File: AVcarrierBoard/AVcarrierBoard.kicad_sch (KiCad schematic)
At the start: 10 parts, among them J1 QuarkScrewTerminal, J2 Screw_Terminal_01x04, J3 Screw_Terminal_01x04, J4 Mech_Switch, J5 Mech_Switch, U1 EggfinderMini/FeatherGPS, U2 EggtimerQuark, U3 Blue_Raven

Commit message: LOST FILES HAHAAHAHA
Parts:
- BT1: value Battery -> Batt_2S; footprint (none) -> COTS_Boards:BAT_1048P
- BT2: value Battery_Cell -> Batt_1S; footprint (none) -> COTS_Boards:1042P_KEY
- J1: value QuarkScrewTerminal -> QuarkRecov; footprint (none) -> COTS_Boards:ScrewTerminals_2828362
- J2: value Screw_Terminal_01x04 -> RavenStaging; footprint (none) -> COTS_Boards:ScrewTerminals_2828362
- J3: value Screw_Terminal_01x04 -> RavenRecov; footprint (none) -> COTS_Boards:ScrewTerminals_2828362
- J4, J5: footprint (none) -> Connector_PinHeader_2.54mm:PinHeader_1x02_P2.54mm_Vertical
- U2: footprint (none) -> COTS_Boards:EggtimerQuark
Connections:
- net BATT_1S: now also J2.2 (Pin_2), J2.4 (Pin_4), J3.2 (Pin_2), J3.4 (Pin_4)
- net RavenAPO: now reaches U3.3 (Apo)
- net RavenAPO: now also J3.3 (Pin_3)
- net RavenMAIN: now reaches U3.4 (Main)
- net RavenMAIN: now also J3.1 (Pin_1)
- net Raven3RD: now reaches U3.5 (3rd)
- net Raven3RD: now also J2.3 (Pin_3)
- net Raven4TH: now reaches U3.6 (4th)
- net Raven4TH: now also J2.1 (Pin_1)
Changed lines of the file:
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@@
+    )
+  )
+  (global_label "Raven3RD" (shape input) (at 135.89 106.68 0) (fields_autoplaced)
+    (effects (font (size 1.27 1.27)) (justify left))
+    (property "Intersheetrefs" "${INTERSHEET_REFS}" (at 148.2489 106.68 0)
+      (effects (font (size 1.27 1.27)) (justify left) hide)
+    )
+  )
+  (global_label "BATT_1S" (shape input) (at 166.37 113.03 180) (fields_autoplaced)
+    (effects (font (size 1.27 1.27)) (justify right))
+    (property "Intersheetrefs" "${INTERSHEET_REFS}" (at 155.7044 113.03 0)
+      (effects (font (size 1.27 1.27)) (justify right) hide)
+    )
+  )
+  (global_label "RavenAPO" (shape input) (at 135.89 111.76 0) (fields_autoplaced)
+    (effects (font (size 1.27 1.27)) (justify left))
+    (property "Intersheetrefs" "${INTERSHEET_REFS}" (at 148.1885 111.76 0)
+      (effects (font (size 1.27 1.27)) (justify left) hide)
+    )
+  )
+  (global_label "RavenAPO" (shape input) (at 166.37 110.49 180) (fields_autoplaced)
+    (effects (font (size 1.27 1.27)) (justify right))
+    (property "Intersheetrefs" "${INTERSHEET_REFS}" (at 154.0715 110.49 0)
+      (effects (font (size 1.27 1.27)) (justify right) hide)
+    )
+  )
+  (global_label "RavenMAIN" (shape input) (at 166.37 105.41 180) (fields_autoplaced)
+    (effects (font (size 1.27 1.27)) (justify right))
+    (property "Intersheetrefs" "${INTERSHEET_REFS}" (at 153.2853 105.41 0)
+      (effects (font (size 1.27 1.27)) (justify right) hide)
+    )
+  )
+  (global_label "BATT_1S" (shape input) (at 166.37 90.17 180) (fields_autoplaced)
+    (effects (font (size 1.27 1.27)) (justify right))
+    (property "Intersheetrefs" "${INTERSHEET_REFS}" (at 155.7044 90.17 0)
+      (effects (font (size 1.27 1.27)) (justify right) hide)
     )
   )
@@
     )
   )
+  (global_label "Raven4TH" (shape input) (at 166.37 87.63 180) (fields_autoplaced)
+    (effects (font (size 1.27 1.27)) (justify right))
+    (property "Intersheetrefs" "${INTERSHEET_REFS}" (at 154.253 87.63 0)
+      (effects (font (size 1.27 1.27)) (justify right) hide)
+    )
+  )
   (global_label "MAIN2" (shape input) (at 132.08 68.58 0) (fields_autoplaced)
     (effects (font (size 1.27 1.27)) (justify left))
@@
     )
   )
+  (global_label "BATT_1S" (shape input) (at 166.37 95.25 180) (fields_autoplaced)
+    (effects (font (size 1.27 1.27)) (justify right))
+    (property "Intersheetrefs" "${INTERSHEET_REFS}" (at 155.7044 95.25 0)
+      (effects (font (size 1.27 1.27)) (justify right) hide)
+    )
+  )
+  (global_label "Raven3RD" (shape input) (at 166.37 92.71 180) (fields_autoplaced)
+    (effects (font (size 1.27 1.27)) (justify right))
+    (property "Intersheetrefs" "${INTERSHEET_REFS}" (at 154.0111 92.71 0)
+      (effects (font (size 1.27 1.27)) (justify right) hide)
+    )
+  )
+  (global_label "BATT_1S" (shape input) (at 166.37 107.95 180) (fields_autoplaced)
+    (effects (font (size 1.27 1.27)) (justify right))
+    (property "Intersheetrefs" "${INTERSHEET_REFS}" (at 155.7044 107.95 0)
+      (effects (font (size 1.27 1.27)) (justify right) hide)
+    )
+  )
   (global_label "+7.5V" (shape input) (at 90.17 66.04 180) (fields_autoplaced)
     (effects (font (size 1.27 1.27)) (justify right))
@@
     )
   )
+  (global_label "RavenMAIN" (shape input) (at 135.89 109.22 0) (fields_autoplaced)
+    (effects (font (size 1.27 1.27)) (justify left))
+    (property "Intersheetrefs" "${INTERSHEET_REFS}" (at 148.9747 109.22 0)
+      (effects (font (size 1.27 1.27)) (justify left) hide)
+    )
+  )
   (global_label "BATT_2S" (shape input) (at 116.84 85.09 180) (fields_autoplaced)
     (effects (font (size 1.27 1.27)) (justify right))
@@
     (property "Intersheetrefs" "${INTERSHEET_REFS}" (at 157.7 72.39 0)
       (effects (font (size 1.27 1.27)) (justify right) hide)
+    )
+  )
+  (global_label "Raven4TH" (shape input) (at 135.89 104.14 0) (fields_autoplaced)
+    (effects (font (size 1.27 1.27)) (justify left))
+    (property "Intersheetrefs" "${INTERSHEET_REFS}" (at 148.007 104.14 0)
+      (effects (font (size 1.27 1.27)) (justify left) hide)
     )
   )
@@
       (effects (font (size 1.27 1.27)) (justify left))
     )
-    (property "Value" "Screw_Terminal_01x04" (at 173.99 110.49 0)
-      (effects (font (size 1.27 1.27)) (justify left))
-    )
-    (property "Footprint" "" (at 171.45 107.95 0)
+    (property "Value" "RavenRecov" (at 173.99 110.49 0)
+      (effects (font (size 1.27 1.27)) (justify left))
+    )
+    (property "Footprint" "COTS_Boards:ScrewTerminals_2828362" (at 171.45 107.95 0)
       (effects (font (size 1.27 1.27)) hide)
     )
@@
       (effects (font (size 1.27 1.27)))
     )
-    (property "Footprint" "" (at 124.46 64.77 0)
+    (property "Footprint" "COTS_Boards:EggtimerQuark" (at 124.46 64.77 0)
       (effects (font (size 1.27 1.27)) hide)
     )
@@
       (effects (font (size 1.27 1.27)) (justify left))
     )
-    (property "Value" "Battery" (at 92.71 85.7885 0)
-      (effects (font (size 1.27 1.27)) (justify left))
-    )
-    (property "Footprint" "" (at 88.9 83.566 90)
+    (property "Value" "Batt_2S" (at 92.71 85.7885 0)
+      (effects (font (size 1.27 1.27)) (justify left))
+    )
+    (property "Footprint" "COTS_Boards:BAT_1048P" (at 88.9 83.566 90)
       (effects (font (size 1.27 1.27)) hide)
     )
@@
       (effects (font (size 1.27 1.27)) (justify left))
     )
-    (property "Value" "Battery_Cell" (at 90.17 127.6985 0)
-      (effects (font (size 1.27 1.27)) (justify left))
-    )
-    (property "Footprint" "" (at 86.36 126.746 90)
+    (property "Value" "Batt_1S" (at 90.17 127.6985 0)
+      (effects (font (size 1.27 1.27)) (justify left))
+    )
+    (property "Footprint" "COTS_Boards:1042P_KEY" (at 86.36 126.746 90)
       (effects (font (size 1.27 1.27)) hide)
     )
@@
       (effects (font (size 1.27 1.27)) (justify left))
     )
-    (property "Value" "QuarkScrewTerminal" (at 173.99 74.93 0)
-      (effects (font (size 1.27 1.27)) (justify left))
-    )
-    (property "Footprint" "" (at 171.45 72.39 0)
+    (property "Value" "QuarkRecov" (at 173.99 74.93 0)
+      (effects (font (size 1.27 1.27)) (justify left))
+    )
+    (property "Footprint" "COTS_Boards:ScrewTerminals_2828362" (at 171.45 72.39 0)
       (effects (font (size 1.27 1.27)) hide)
     )
@@
       (effects (font (size 1.27 1.27)) (justify left))
     )
-    (property "Footprint" "" (at 95.25 63.5 0)
+    (property "Footprint" "Connector_PinHeader_2.54mm:PinHeader_1x02_P2.54mm_Vertical" (at 95.25 63.5 0)
       (effects (font (size 1.27 1.27)) hide)
     )
@@
       (effects (font (size 1.27 1.27)) (justify left))
     )
-    (property "Footprint" "" (at 93.98 104.14 0)
+    (property "Footprint" "Connector_PinHeader_2.54mm:PinHeader_1x02_P2.54mm_Vertical" (at 93.98 104.14 0)
       (effects (font (size 1.27 1.27)) hide)
     )
@@
       (effects (font (size 1.27 1.27)) (justify left))
     )
-    (property "Value" "Screw_Terminal_01x04" (at 173.99 92.71 0)
-      (effects (font (size 1.27 1.27)) (justify left))
-    )
-    (property "Footprint" "" (at 171.45 90.17 0)
-      (effects (font (size 1.27 1.27)) hide)
-    )
+    (property "Value" "RavenStaging" (at 173.99 92.71 0)
+      (effects (font (size 1.27 1.27)) (justify left))
+    )
+    (property "Footprint" "COTS_Boards:ScrewTerminals_2828362" (at 171.45 90.17 0)
+      (effects (font (size 1.27 1.27)) hide)
+    )

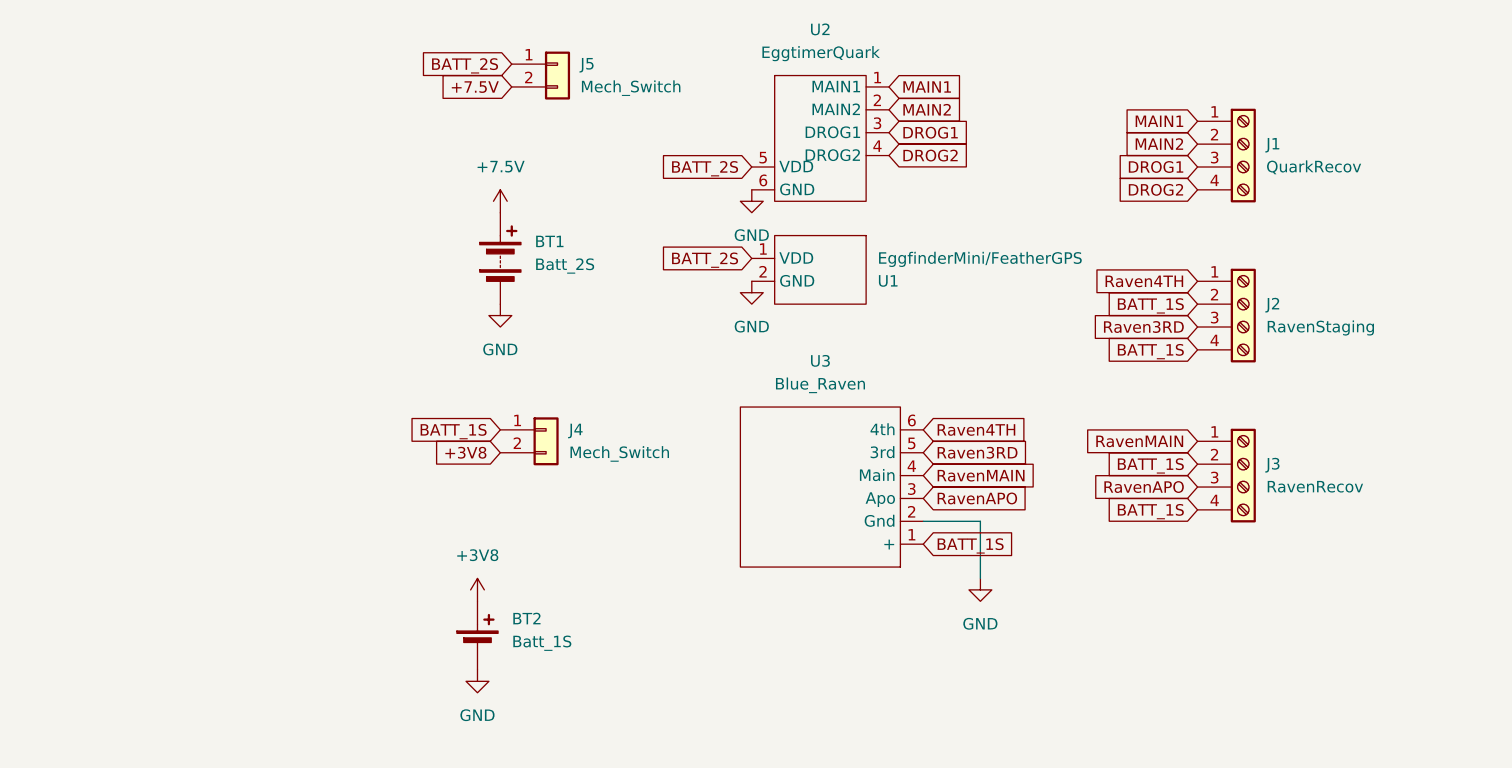
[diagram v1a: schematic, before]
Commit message: Added wifi switch into schematic
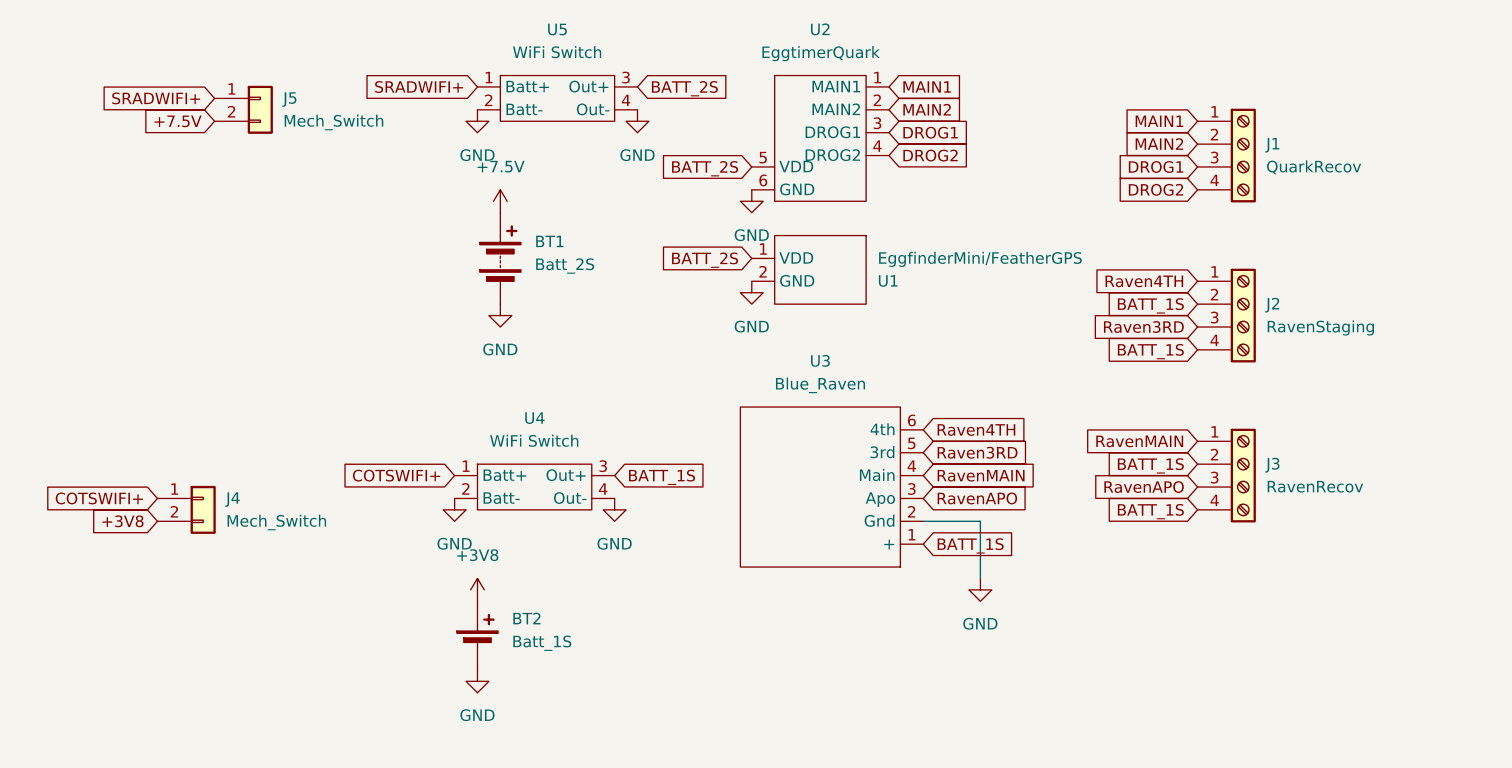
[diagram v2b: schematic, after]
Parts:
- added U4, U5: WiFi Switch, symbol COTS_boards:Eggtimer_WiFi_switch
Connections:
- net BATT_1S: now also U4.3 (Out+); no longer J4.1 (Pin_1)
- net BATT_2S: now also U5.3 (Out+); no longer J5.1 (Pin_1)
- net GND: now also U4.2 (Batt-), U4.4 (Out-), U5.2 (Batt-), U5.4 (Out-)
- new net COTSWIFI+: J4.1 (Pin_1), U4.1 (Batt+)
- new net SRADWIFI+: J5.1 (Pin_1), U5.1 (Batt+)
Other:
- moved on the sheet: J4, J5
